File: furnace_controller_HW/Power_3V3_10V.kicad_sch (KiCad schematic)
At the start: 31 parts, among them Q1 BC847, Q2 IRLML6402, Q3 IRLML2402, U1 AMS1117-3.3

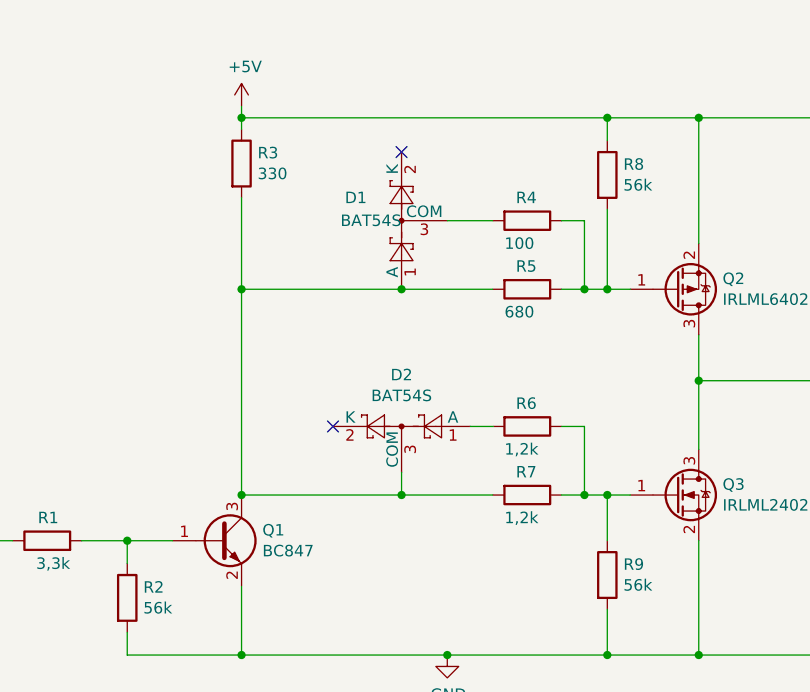
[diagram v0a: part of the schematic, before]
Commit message: Tune resistor values for the proper charge pump MOSFETs deadtime
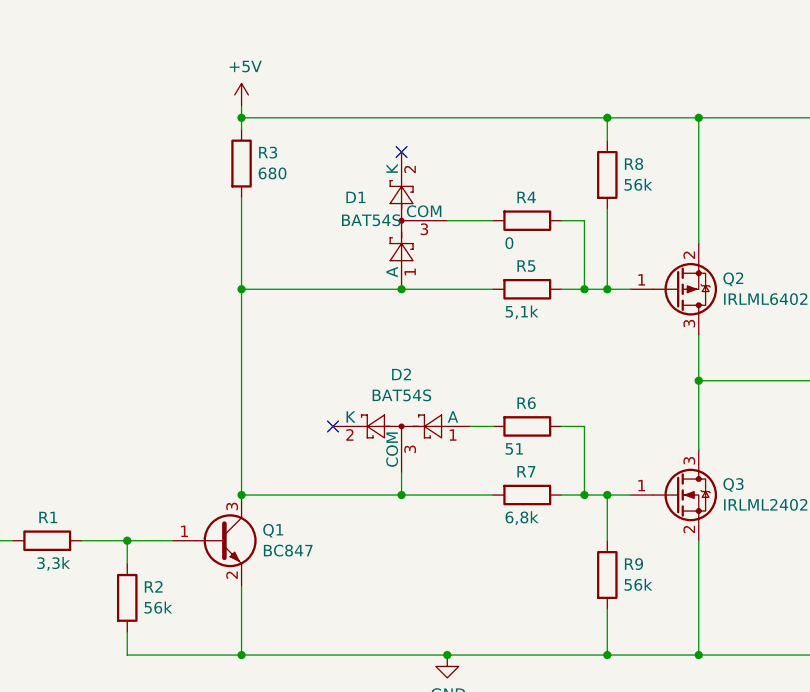
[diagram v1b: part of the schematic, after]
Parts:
- R3: value 330 -> 680
- R4: value 100 -> 0
- R5: value 680 -> 5,1k
- R6: value 1,2k -> 51
- R7: value 1,2k -> 6,8k
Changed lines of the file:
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@@
 			)
 		)
-		(property "Value" "100"
+		(property "Value" "0"
 			(at 143.51 113.03 90)
 			(effects
@@
 			)
 		)
-		(property "Value" "680"
+		(property "Value" "5,1k"
 			(at 143.51 120.65 90)
 			(effects
@@
 			)
 		)
-		(property "Value" "1,2k"
+		(property "Value" "51"
 			(at 143.51 135.89 90)
 			(effects
@@
 			)
 		)
-		(property "Value" "1,2k"
+		(property "Value" "6,8k"
 			(at 143.51 143.51 90)
 			(effects
@@
 			)
 		)
-		(property "Value" "330"
+		(property "Value" "680"
 			(at 116.078 105.283 0)
 			(effects
